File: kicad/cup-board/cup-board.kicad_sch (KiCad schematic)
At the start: 98 parts, among them J2 EARCUP_SPKR, J5 XF_SEC_FROM_AUDIO_BOARD, J7 A2B_A (from AeroNode / previo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, J8 A2B_B (to next cup), Q1 AO3401A, Q2 MMBT3904, U1 ADAU1861, U2 LSM6DSV16BX, U3 MAXM86161, U4 AQW612S, U5 AQW612S, U6 AD2428WBCPZ (sub-node), U7 TPS62161DSG (1V8), U8 ADP7118AUJZ-3.3-R7 (3V3_MIC), U9 ADP7118AUJZ-3.3-R7 (VLED)

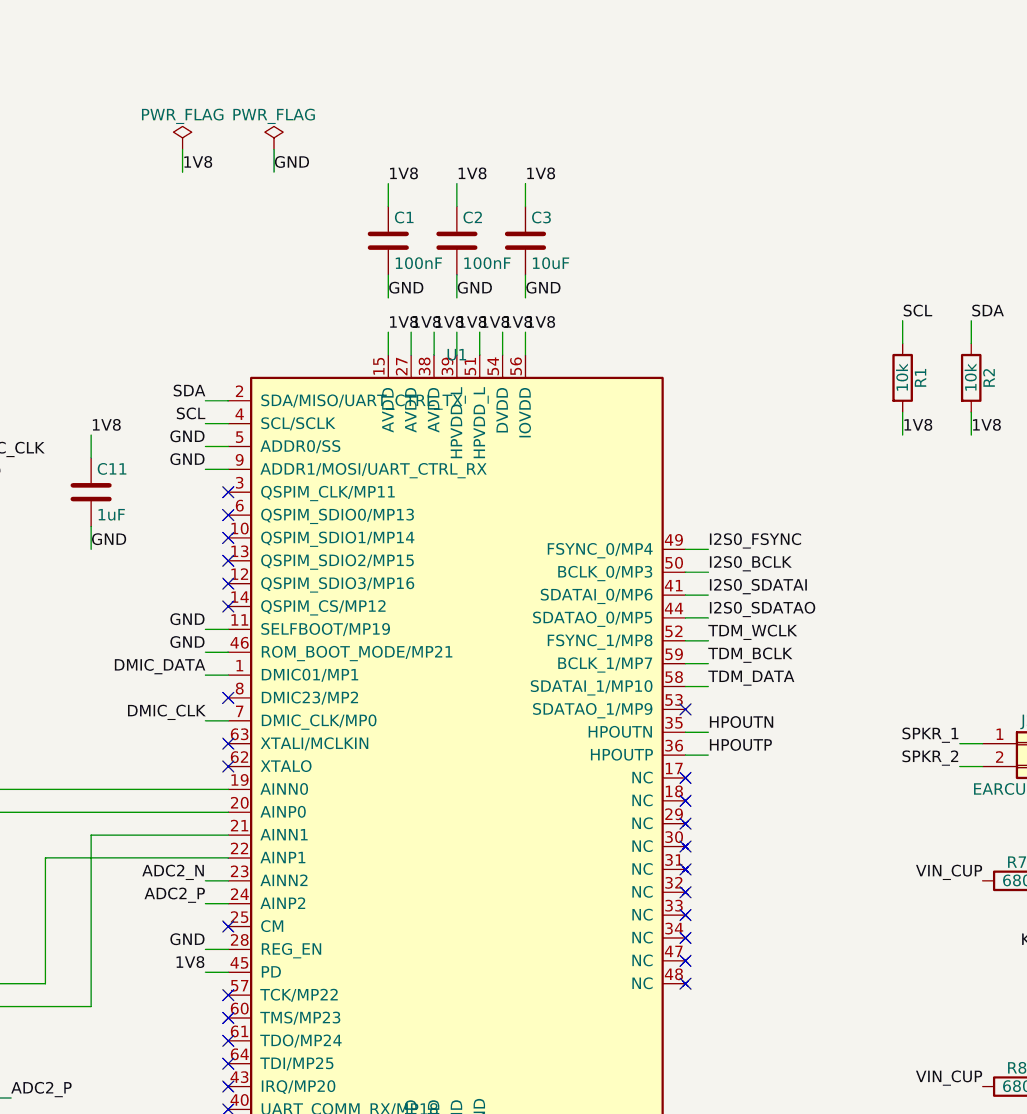
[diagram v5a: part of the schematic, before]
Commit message: [LIMA] cup board: fix U1 DVDD overvoltage - ADAU1861 internal regulator on
U1 pin 54 (DVDD) was on the 1V8 rail against a 1.21 V absolute maximum
(ADAU1861 DS: DVDD 0.85-1.21 V, abs max -0.3 to +1.21 V), with pin 28
REG_EN grounded. Now per the DS pin table: REG_EN tied to AVDD (1V8), DVDD
on its own net U1_DVDD with C47 1 uF + C48 100 nF to ground, PWR_FLAG for
the internally driven rail. Peter approved the fix 2026-10-26.

Checked: netlist == doc/design_nets.py; ERC 0 errors (6 strap warnings,
unchanged).

Co-Authored-By: Claude Opus 5.5 <noreply@anthropic.com>
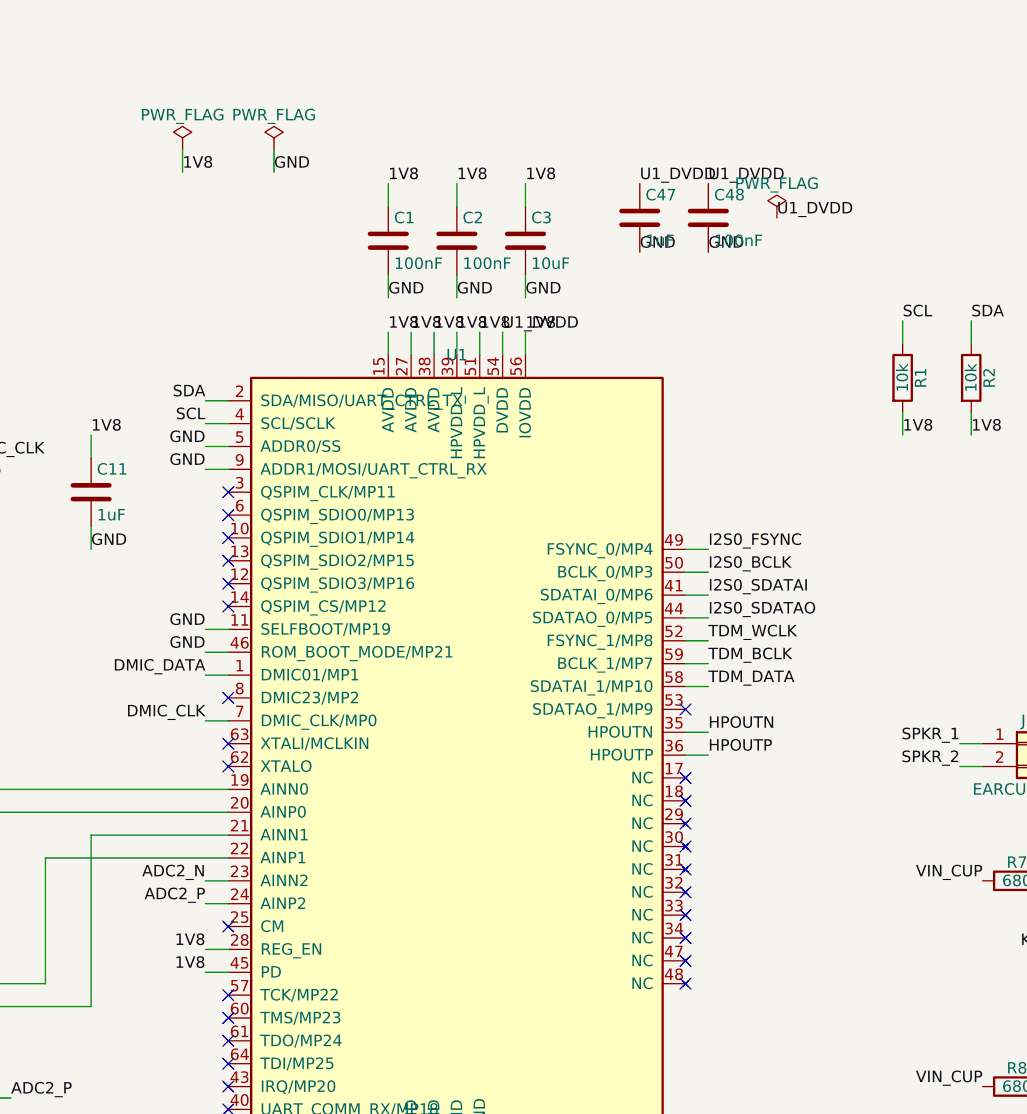
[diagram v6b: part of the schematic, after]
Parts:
- added C47: 1uF, symbol Device:C
- added C48: 100nF, symbol Device:C
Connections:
- net 1V8: now also U1.28 (REG_EN); no longer U1.54 (DVDD)
- net GND: now also C47.2, C48.2; no longer U1.28 (REG_EN)
- new net U1_DVDD: C47.1, C48.1, U1.54 (DVDD)
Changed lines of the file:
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@@
 		)
 	)
+	(text "A2B SUB-NODE (2026-10-23, per Peter): U6 AD2428, bus-powered (AD242x DS Fig. 36; coupling per EVAL-AD2428WD1BZ sheet 2)\nA side J7 (from AeroNode or previous cup): line+ -> L3 -> V_NODE -> D1 -> VIN_CUP; line- -> L4 -> GND (this cup's ground is the recovered bus bias).\nB side J8 (to next cup, unused on the last cup): V_NODE -> R12 -> Q1 (gate: SWP via R13) -> L5 -> line+; line- -> L6 -> VSSN. SENSE via R14.\nI2S: U6 is master. DTX0 -> I2S0_SDATAI (ADAU1861 in), DRX0 <- I2S0_SDATAO. I2C: U6 masters SDA/SCL at 1V8 (IOVDD = 1V8).\nK2: AudioBoard CTL_SPKR -> main IO7 -> GPIO-over-distance -> U6 IO7 -> K2_CTL -> Q2 -> U4/U5 LEDs (R7/R8 680R from VIN_CUP). Default off.\nPower from VIN_CUP (6.4-7.2 V with the AeroNode's 8 V bus): U7 TPS62161 -> 1V8; U8 ADP7118 -> 3V3_MIC; U9 ADP7118 -> VLED.\nEE-419: a bus-powered node's ground is offset from the AeroNode's - connect only floating signals (J5 is transformer-isolated, AC-coupled).\nBudget: docs/a2b-bus-power-budget.md - cup R VIN 6.44 V worst case on the 8 V bus (3.7 V min)."
+		(at 475 285 0)
+		(effects
+			(font
+				(size 1.524 1.524)
+			)
+		)
+	)
 	(label "1V8"
 		(at 160.02 82.55 0)
@@
 	)
 	(label "1V8"
-		(at 195.58 100.33 0)
-		(effects
-			(font
-				(size 1.27 1.27)
-			)
-			(justify left bottom)
-		)
-	)
-	(label "1V8"
 		(at 198.12 100.33 0)
 		(effects
@@
 		)
 	)
-	(label "GND"
-		(at 162.56 168.91 180)
-		(effects
-			(font
-				(size 1.27 1.27)
-			)
-			(justify right bottom)
-		)
-	)
 	(label "1V8"
 		(at 162.56 171.45 180)
@@
 		)
 	)
-  (text "A2B SUB-NODE (2026-10-23, per Peter): U6 AD2428, bus-powered (AD242x DS Fig. 36; coupling per EVAL-AD2428WD1BZ sheet 2)\nA side J7 (from AeroNode or previous cup): line+ -> L3 -> V_NODE -> D1 -> VIN_CUP; line- -> L4 -> GND (this cup's ground is the recovered bus bias).\nB side J8 (to next cup, unused on the last cup): V_NODE -> R12 -> Q1 (gate: SWP via R13) -> L5 -> line+; line- -> L6 -> VSSN. SENSE via R14.\nI2S: U6 is master. DTX0 -> I2S0_SDATAI (ADAU1861 in), DRX0 <- I2S0_SDATAO. I2C: U6 masters SDA/SCL at 1V8 (IOVDD = 1V8).\nK2: AudioBoard CTL_SPKR -> main IO7 -> GPIO-over-distance -> U6 IO7 -> K2_CTL -> Q2 -> U4/U5 LEDs (R7/R8 680R from VIN_CUP). Default off.\nPower from VIN_CUP (6.4-7.2 V with the AeroNode's 8 V bus): U7 TPS62161 -> 1V8; U8 ADP7118 -> 3V3_MIC; U9 ADP7118 -> VLED.\nEE-419: a bus-powered node's ground is offset from the AeroNode's - connect only floating signals (J5 is transformer-isolated, AC-coupled).\nBudget: docs/a2b-bus-power-budget.md - cup R VIN 6.44 V worst case on the 8 V bus (3.7 V min)."
-    (at 475 285 0)
-    (effects (font (size 1.524 1.524)))
+	(label "U1_DVDD"
+		(at 195.58 100.33 0)
+		(effects
+			(font
+				(size 1.27 1.27)
+			)
+			(justify left bottom)
+		)
+	)
+	(label "1V8"
+		(at 162.56 168.91 180)
+		(effects
+			(font
+				(size 1.27 1.27)
+			)
+			(justify right bottom)
+		)
+	)
+	(label "U1_DVDD"
+		(at 210.82 83.82 0)
+		(effects
+			(font
+				(size 1.27 1.27)
+			)
+			(justify left bottom)
+		)
+	)
+	(label "U1_DVDD"
+		(at 218.44 83.82 0)
+		(effects
+			(font
+				(size 1.27 1.27)
+			)
+			(justify left bottom)
+		)
+	)
+	(label "GND"
+		(at 210.82 91.44 0)
+		(effects
+			(font
+				(size 1.27 1.27)
+			)
+			(justify left bottom)
+		)
+	)
+	(label "GND"
+		(at 218.44 91.44 0)
+		(effects
+			(font
+				(size 1.27 1.27)
+			)
+			(justify left bottom)
+		)
+	)
+  (label "U1_DVDD"
+    (at 226.06 87.63 0)
+    (fields_autoplaced yes)
+    (effects (font (size 1.27 1.27)) (justify left bottom))
   )
 	(symbol
@@
 					(unit 1)
 				)
+			)
+		)
+	)
+	(symbol
+		(lib_id "Device:C")
+		(at 210.82 87.63 0)
+		(unit 1)
+		(in_bom yes)
+		(on_board yes)
+		(dnp no)
+		(property "Reference" "C47"
+			(at 211.455 85.09 0)
+			(effects
+				(font
+					(size 1.27 1.27)
+				)
+				(justify left)
+			)
+		)
+		(property "Value" "1uF"
+			(at 211.455 90.17 0)
+			(effects
+				(font
+					(size 1.27 1.27)
+				)
+				(justify left)
+			)
+		)
+		(property "Footprint" ""
+			(at 210.82 87.63 0)
+			(hide yes)
+			(effects
+				(font
+					(size 1.27 1.27)
+				)
+			)
+		)
+		(property "Datasheet" ""
+			(at 210.82 87.63 0)
+			(hide yes)
+			(effects
+				(font
+					(size 1.27 1.27)
+				)
+			)
+		)
+		(instances
+			(project "cup-board"
+				(path "790ac8fa-b8c8-432b-bc66-3eedd04170ff"
+					(reference "C47")
+					(unit 1)
+				)
+			)
+		)
+	)
+	(symbol
+		(lib_id "Device:C")
+		(at 218.44 87.63 0)
+		(unit 1)
+		(in_bom yes)
+		(on_board yes)
+		(dnp no)
+		(property "Reference" "C48"
+			(at 219.075 85.09 0)
+			(effects
+				(font
+					(size 1.27 1.27)
+				)
+				(justify left)
+			)
+		)
+		(property "Value" "100nF"
+			(at 219.075 90.17 0)
+			(effects
+				(font
+					(size 1.27 1.27)
+				)
+				(justify left)
+			)
+		)
+		(property "Footprint" ""
+			(at 218.44 87.63 0)
+			(hide yes)
+			(effects
+				(font
+					(size 1.27 1.27)
+				)
+			)
+		)
+		(property "Datasheet" ""
+			(at 218.44 87.63 0)
+			(hide yes)
+			(effects
+				(font
+					(size 1.27 1.27)
+				)
+			)
+		)
+		(instances
+			(project "cup-board"
+				(path "790ac8fa-b8c8-432b-bc66-3eedd04170ff"
+					(reference "C48")
+					(unit 1)
+				)
+			)
+		)
+	)
+	(symbol
+		(lib_id "power:PWR_FLAG")
+		(at 226.06 87.63 0)
+		(unit 1)
+		(in_bom yes)
+		(on_board yes)
+		(dnp no)
+		(property "Reference" "#FLG10"
+			(at 226.06 85.725 0)
+			(hide yes)
+			(effects
+				(font
+					(size 1.27 1.27)
+				)
+			)
+		)
+		(property "Value" "PWR_FLAG"
+			(at 226.06 83.82 0)
+			(effects
+				(font
+					(size 1.27 1.27)
+				)
+			)
+		)
+		(property "Footprint" ""
+			(at 226.06 87.63 0)
+			(hide yes)
+			(effects
+				(font
+					(size 1.27 1.27)
+				)
+			)
+		)
+		(property "Datasheet" ""
+			(at 226.06 87.63 0)
+			(hide yes)
+			(effects
+				(font
+					(size 1.27 1.27)
+				)
+			)
+		)
+		(instances
+			(project "cup-board"
+				(path "/790ac8fa-b8c8-432b-bc66-3eedd04170ff"
+					(reference "#FLG10")
+					(unit 1)
+				)

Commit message: [LIMA] cup board: connectors match the audio board; PPG_INT to A2B IO0
- J5 merged into J7: 4-pin JST GH, 1 A_LINE_P, 2 A_LINE_N, 3/4 SP-74
  secondary - same order as audio J3, straight 1:1 cable to cup L. J8 (A2B
  out) and J2 (speaker) now JST GH 2-pin. Cup R takes a split harness into
  J7 (A2B from cup L J8, speaker pair from audio J4).
- PPG_INT (MAXM86161 INTB) -> U6 IRQ/IO0, GPIO input with interrupt in
  slave mode (AD242x DS Table 15); 1V8 levels on both sides.
- README: dated section for the 2026-10-26 changes; DVDD and PPG_INT
  open items closed.

Checked: netlist == doc/design_nets.py, ERC 0 errors (6 strap warnings).

Co-Authored-By: Claude Opus 5.5 <noreply@anthropic.com>
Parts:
- removed J5: XF_SEC_FROM_AUDIO_BOARD, symbol Connector_Generic:Conn_01x02
- removed J7: A2B_A (from AeroNode / previous cup), symbol Connector_Generic:Conn_01x02
- added J7: CUP_IN (A2B + panel audio, mates audio J3), Connector_JST:JST_GH_SM04B-GHS-TB_1x04-1MP_P1.25mm_Horizontal, symbol Connector_Generic:Conn_01x04
- J2: footprint (none) -> Connector_JST:JST_GH_SM02B-GHS-TB_1x02-1MP_P1.25mm_Horizontal
- J8: value A2B_B (to next cup) -> CUP_OUT (A2B to next cup); footprint (none) -> Connector_JST:JST_GH_SM02B-GHS-TB_1x02-1MP_P1.25mm_Horizontal
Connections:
- net A_LINE_N: now also J7.2 (Pin_2)
- net A_LINE_P: now also J7.1 (Pin_1)
- net PPG_INT: now also U6.6 (IRQ/IO0)
- net XF_SEC_A: now also J7.3 (Pin_3)
- net XF_SEC_B: now also J7.4 (Pin_4)
- no-connect marks 38 -> 37
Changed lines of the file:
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@@
 	)
 	(no_connect
-		(at 431.8 111.76)
-	)
-	(no_connect
 		(at 431.8 127)
 	)
@@
 	(wire
 		(pts
-			(xy 93.98 194.31)
-			(xy 91.44 194.31)
-		)
-	)
-	(wire
-		(pts
-			(xy 93.98 196.85)
-			(xy 91.44 196.85)
-		)
-	)
-	(wire
-		(pts
 			(xy 118.11 185.42)
 			(xy 115.57 185.42)
@@
 		)
 	)
-	(label "XF_SEC_A"
-		(at 91.44 194.31 180)
-		(effects
-			(font
-				(size 1.27 1.27)
-			)
-			(justify right bottom)
-		)
-	)
-	(label "XF_SEC_B"
-		(at 91.44 196.85 180)
-		(effects
-			(font
-				(size 1.27 1.27)
-			)
-			(justify right bottom)
-		)
-	)
 	(label "1V8"
 		(at 142.24 309.88 0)
@@
 		)
 	)
-  (label "U1_DVDD"
-    (at 226.06 87.63 0)
+	(label "U1_DVDD"
+		(at 226.06 87.63 0)
+		(effects
+			(font
+				(size 1.27 1.27)
+			)
+			(justify left bottom)
+		)
+	)
+  (label "XF_SEC_A"
+    (at 490.22 226.06 180)
+    (fields_autoplaced yes)
+    (effects (font (size 1.27 1.27)) (justify right bottom))
+  )
+  (label "XF_SEC_B"
+    (at 490.22 228.60000000000002 180)
+    (fields_autoplaced yes)
+    (effects (font (size 1.27 1.27)) (justify right bottom))
+  )
+  (label "PPG_INT"
+    (at 431.8 111.76 0)
     (fields_autoplaced yes)
     (effects (font (size 1.27 1.27)) (justify left bottom))
@@
 			)
 		)
-		(property "Footprint" ""
+		(property "Footprint" "Connector_JST:JST_GH_SM02B-GHS-TB_1x02-1MP_P1.25mm_Horizontal"
 			(at 254 146.05 0)
 			(hide yes)
@@
 	)
 	(symbol
-		(lib_id "Connector_Generic:Conn_01x02")
-		(at 99.06 194.31 0)
-		(unit 1)
-		(in_bom yes)
-		(on_board yes)
-		(dnp no)
-		(property "Reference" "J5"
-			(at 99.06 191.77 0)
-			(effects
-				(font
-					(size 1.27 1.27)
-				)
-			)
-		)
-		(property "Value" "XF_SEC_FROM_AUDIO_BOARD"
-			(at 99.06 199.39 0)
-			(effects
-				(font
-					(size 1.27 1.27)
-				)
-			)
-		)
-		(property "Footprint" ""
-			(at 99.06 194.31 0)
-			(hide yes)
-			(effects
-				(font
-					(size 1.27 1.27)
-				)
-			)
-		)
-		(property "Datasheet" ""
-			(at 99.06 194.31 0)
-			(hide yes)
-			(effects
-				(font
-					(size 1.27 1.27)
-				)
-			)
-		)
-		(instances
-			(project "cup-board"
-				(path "/790ac8fa-b8c8-432b-bc66-3eedd04170ff"
-					(reference "J5")
-					(unit 1)
-				)
-			)
-		)
-	)
-	(symbol
 		(lib_id "Device:C")
 		(at 121.92 185.42 90)
@@
 			)
 		)
-		(property "Value" "A2B_B (to next cup)"
+		(property "Value" "CUP_OUT (A2B to next cup)"
 			(at 525.78 152.4 0)
 			(effects
@@
 			)
 		)
-		(property "Footprint" ""
+		(property "Footprint" "Connector_JST:JST_GH_SM02B-GHS-TB_1x02-1MP_P1.25mm_Horizontal"
 			(at 525.78 147.32 0)
 			(hide yes)
@@
 	)
 	(symbol
-		(lib_id "Connector_Generic:Conn_01x02")
-		(at 495.3 220.98 0)
-		(unit 1)
-		(in_bom yes)
-		(on_board yes)
-		(dnp no)
-		(property "Reference" "J7"
-			(at 495.3 218.44 0)
-			(effects
-				(font
-					(size 1.27 1.27)
-				)
-			)
-		)
-		(property "Value" "A2B_A (from AeroNode / previous cup)"
-			(at 495.3 226.06 0)
-			(effects
-				(font
-					(size 1.27 1.27)
-				)
-			)
-		)
-		(property "Footprint" ""
-			(at 495.3 220.98 0)
-			(hide yes)
-			(effects
-				(font
-					(size 1.27 1.27)
-				)
-			)
-		)
-		(property "Datasheet" ""
-			(at 495.3 220.98 0)
-			(hide yes)
-			(effects
-				(font
-					(size 1.27 1.27)
-				)
-			)
-		)
-		(instances
-			(project "cup-board"
-				(path "790ac8fa-b8c8-432b-bc66-3eedd04170ff"
-					(reference "J7")
-					(unit 1)
-				)
-			)
-		)
-	)
-	(symbol
 		(lib_id "Device:D_Schottky")
 		(at 525.78 220.98 0)
@@
 					(unit 1)
 				)
+			)
+		)
+	)
+	(symbol
+		(lib_id "Connector_Generic:Conn_01x04")
+		(at 495.3 223.52 0)
+		(unit 1)
+		(in_bom yes)
+		(on_board yes)
+		(dnp no)
+		(property "Reference" "J7"
+			(at 495.3 218.44 0)
+			(effects
+				(font
+					(size 1.27 1.27)
+				)
+			)
+		)
+		(property "Value" "CUP_IN (A2B + panel audio, mates audio J3)"
+			(at 495.3 231.14 0)
+			(effects
+				(font
+					(size 1.27 1.27)
+				)
+			)
+		)
+		(property "Footprint" "Connector_JST:JST_GH_SM04B-GHS-TB_1x04-1MP_P1.25mm_Horizontal"
+			(at 495.3 223.52 0)
+			(hide yes)
+			(effects
+				(font
+					(size 1.27 1.27)
+				)
+			)
+		)
+		(property "Datasheet" ""
+			(at 495.3 223.52 0)
+			(hide yes)
+			(effects
+				(font
+					(size 1.27 1.27)
+				)
+			)
+		)
+		(instances
+			(project "cup-board"
+				(path "/790ac8fa-b8c8-432b-bc66-3eedd04170ff"
+					(reference "J7")
+					(unit 1)
+				)

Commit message: [LIMA] cup board: footprints for 116 of 117 parts (U3 MAXM86161 pending)
New: ADAU1861 CS-64-2 (ADI recommended pad layout, DS p.28) and one shared
Infineon 4x3 LLGA-5 for IM73A135 x2 + IM72D128 (same land pattern and
numbering, plated sound port). Stock: LGA-14 3x2.5 for LSM6DSV16BX (matches
DS Fig. 31), QFN-32 for AD2428, WSON/TSOT/SOT parts, JST GH connectors;
AQW612S reused from the audio board. Passives 0603.

Checked: netlist == design_nets.py, ERC 0 errors, symbol-pin/footprint-pad
parity 0 mismatches. U3 waits for Maxim land pattern 90-100106 (not in the
datasheet) - not guessed.

Co-Authored-By: Claude Opus 5.5 <noreply@anthropic.com>
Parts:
- C1, C10, C11, C12, C13, C14, C15, C16, C17, C18, C19, C2, C20, C21, C22, C24, C25, C26, C27, C28, C29, C30, C31, C32, C33, C34, C35, C36, C37, C38, C39, C4, C40, C43, C44, C45, C46, C47, C48, C5, C7, C8, C9: footprint (none) -> Capacitor_SMD:C_0603_1608Metric
- C23, C3, C41, C42, C6: footprint (none) -> Capacitor_SMD:C_0805_2012Metric
- D1: footprint (none) -> Diode_SMD:D_SOD-323
- FB1, FB2, FB3, FB4, L1, L2, L7, L8: footprint (none) -> Inductor_SMD:L_0603_1608Metric
- FL1, FL2: footprint (none) -> Inductor_SMD:L_CommonModeChoke_Coilank_ACM3216
- L3, L4, L5, L6: footprint (none) -> Inductor_SMD:L_1210_3225Metric
- L9: footprint (none) -> Inductor_SMD:L_1008_2520Metric
- MK1, MK2, MK3: footprint (none) -> Infineon:Infineon_PG-LLGA-5_4x3mm_IM73A135_IM72D128
- Q1, Q2: footprint (none) -> Package_TO_SOT_SMD:SOT-23
- R1, R10, R11, R13, R14, R15, R16, R17, R18, R2, R3, R4, R5, R6, R7, R8, R9: footprint (none) -> Resistor_SMD:R_0603_1608Metric
- R12: footprint (none) -> Resistor_SMD:R_1206_3216Metric
- U1: footprint (none) -> AnalogDevices:AD_LFCSP-SS-64-1EP_9x9mm_P0.5mm_EP6.3x6.3mm_CS-64-2
- U2: footprint (none) -> Package_LGA:LGA-14_3x2.5mm_P0.5mm_LayoutBorder3x4y
- U4, U5: footprint (none) -> Panasonic:Panasonic_GU-SOP8_4.4x9.37mm_P2.54mm_AQW61xS
- U6: footprint (none) -> Package_DFN_QFN:QFN-32-1EP_5x5mm_P0.5mm_EP3.6x3.6mm_ThermalVias
- U7: footprint (none) -> Package_SON:WSON-8-1EP_2x2mm_P0.5mm_EP0.9x1.6mm_ThermalVias
- U8, U9: footprint (none) -> Package_TO_SOT_SMD:TSOT-23-5
